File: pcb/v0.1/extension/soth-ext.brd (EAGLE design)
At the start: 50 x 18.9 mm, 5 parts, among them IC1 MPU-9250, IC2 BME280

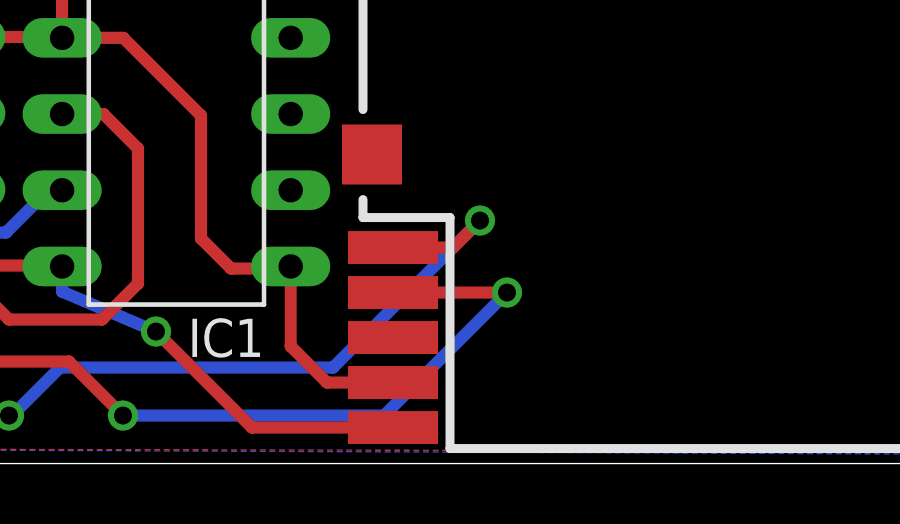
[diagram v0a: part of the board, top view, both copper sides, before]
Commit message: Successfully gps data rcv.
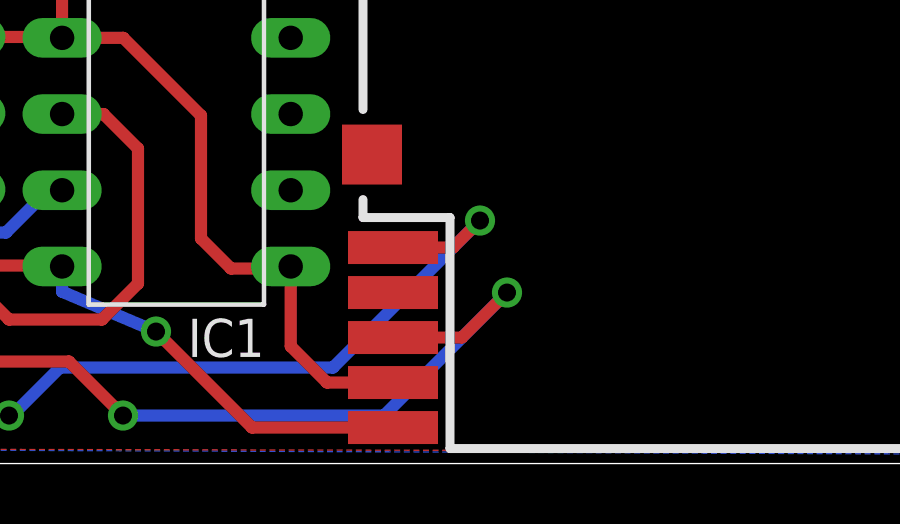
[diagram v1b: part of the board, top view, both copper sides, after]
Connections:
- net N$3: now also U$1.TX; no longer U$1.RX
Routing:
- net N$3: track 35.7 -> 36.4 mm
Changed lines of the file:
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@@
 <signal name="N$3">
 <contactref element="JP1" pad="5"/>
-<contactref element="U$1" pad="RX"/>
 <wire x1="2.26" y1="4.01" x2="13.59" y2="4.01" width="0.4064" layer="1"/>
 <wire x1="13.59" y1="4.01" x2="14.2" y2="3.4" width="0.4064" layer="1"/>
@@
 <wire x1="27.4" y1="1.6" x2="31.5" y2="5.7" width="0.4064" layer="16"/>
 <via x="31.5" y="5.7" extent="1-16" drill="0.6"/>
-<wire x1="31.5" y1="5.7" x2="27.7" y2="5.7" width="0.4064" layer="1"/>
+<contactref element="U$1" pad="TX"/>
+<wire x1="27.7" y1="4.2" x2="30" y2="4.2" width="0.4" layer="1"/>
+<wire x1="30" y1="4.2" x2="31.5" y2="5.7" width="0.4" layer="1"/>
 </signal>
 <signal name="N$4">
